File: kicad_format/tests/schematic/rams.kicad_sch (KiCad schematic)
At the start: 8 parts, among them U12 SIM4X32, U13 SIM4X32, U14 SIM4X32, U15 SIM4X32, U16 SIM4X32, U17 SIM4X32, U18 SIM4X32, U19 SIM4X32

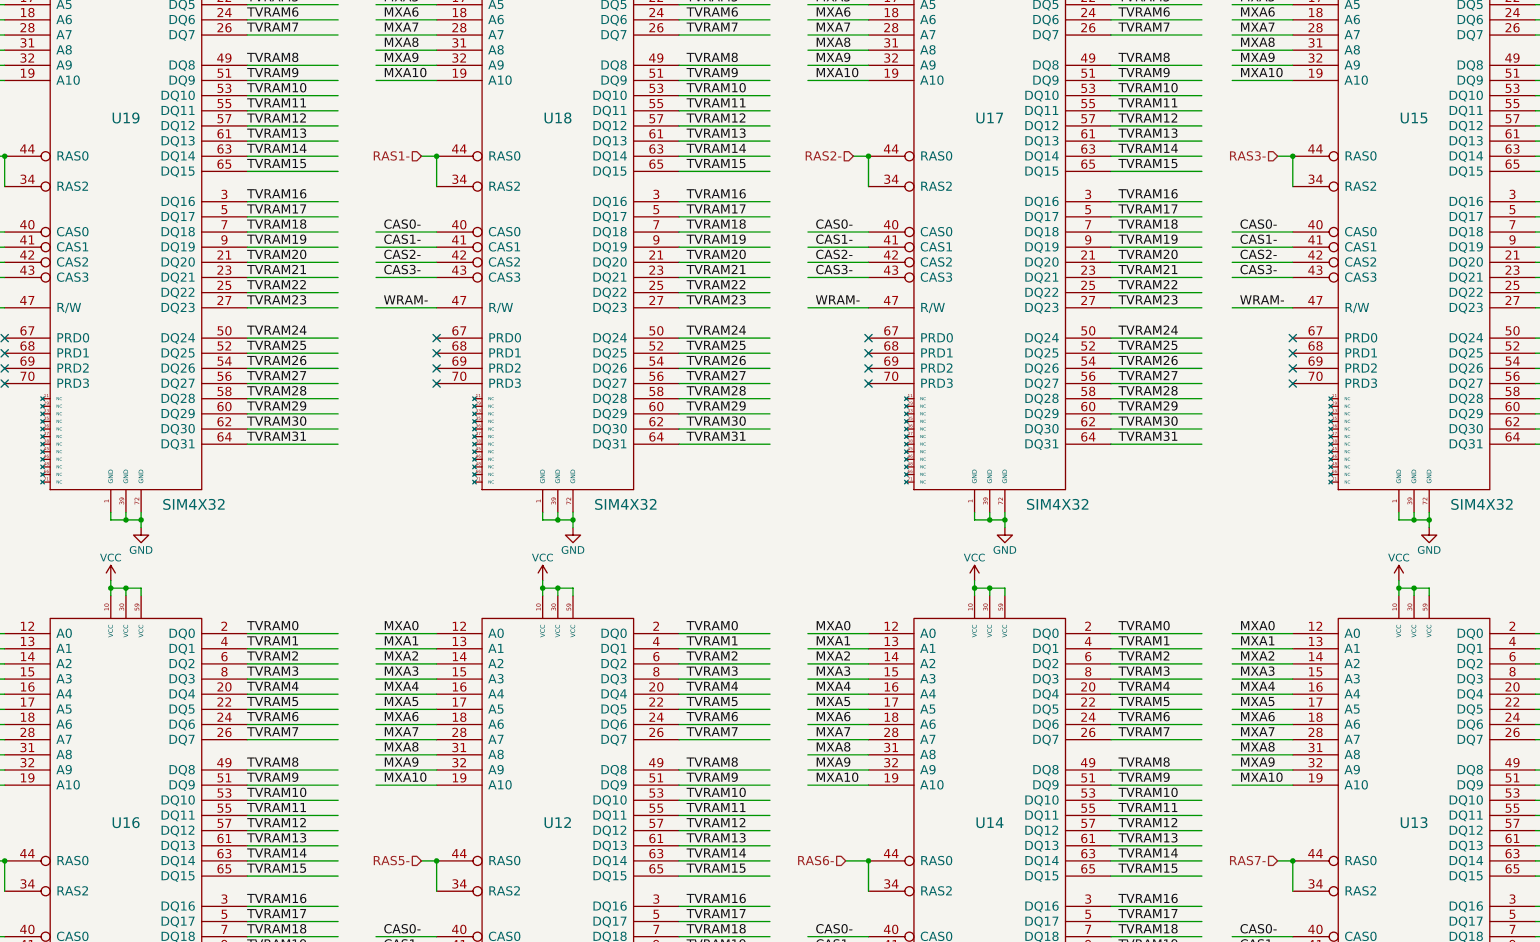
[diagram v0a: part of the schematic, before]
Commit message: Add serialization context and support most modern kicad file idiosyncrasies
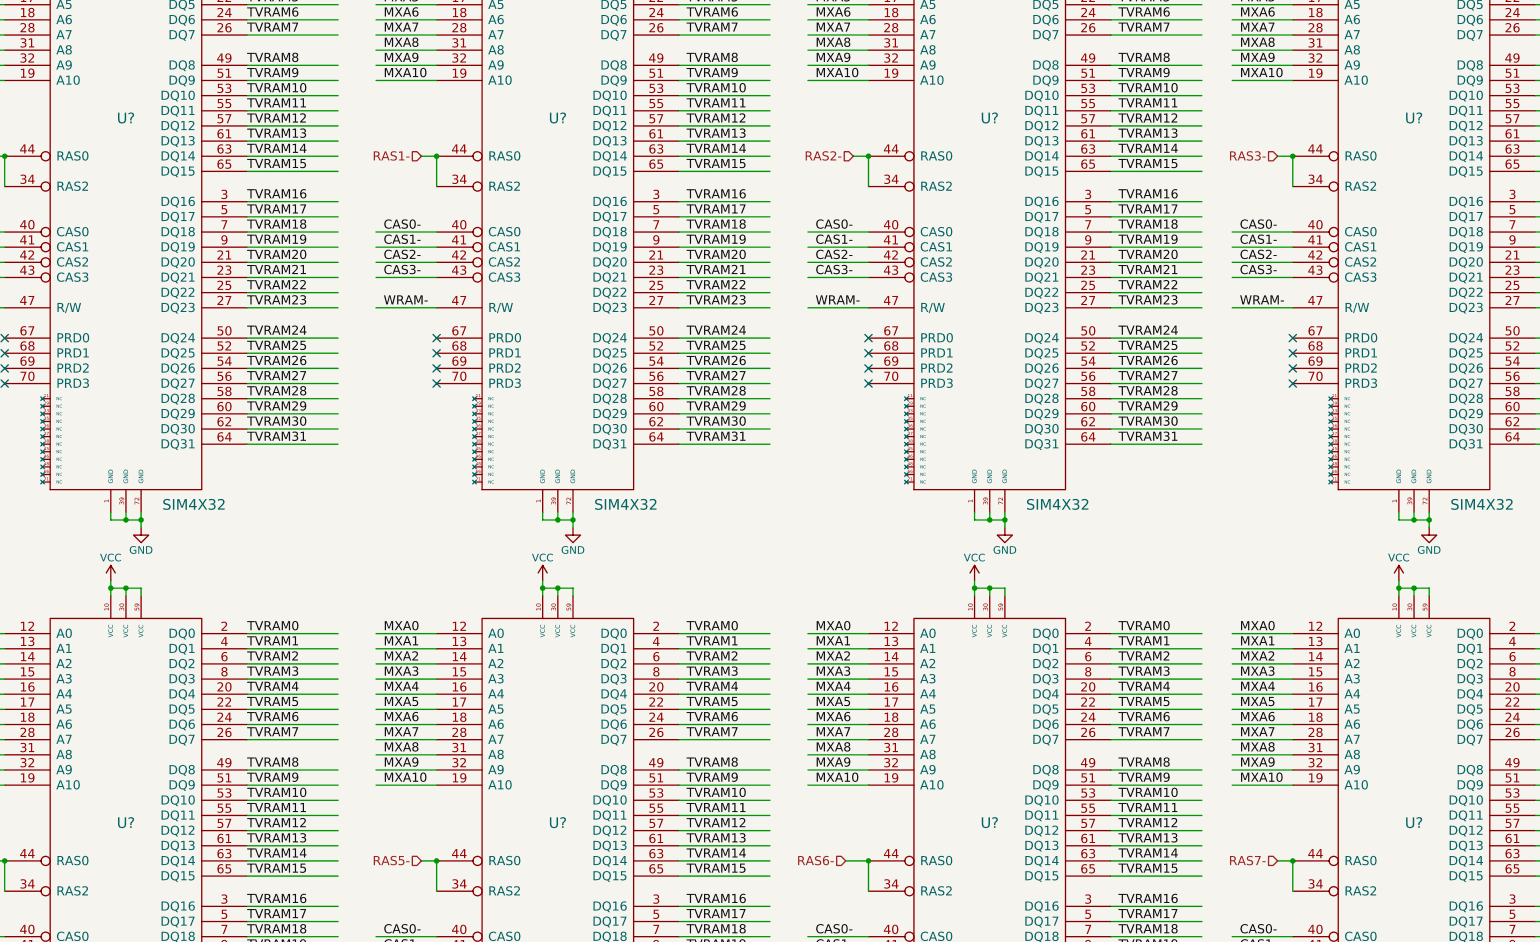
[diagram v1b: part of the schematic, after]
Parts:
- renumbered U13 to U?, U12 to U?, U14 to U?, U16 to U?, U15 to U?, U17 to U?, U18 to U?, U19 to U?
